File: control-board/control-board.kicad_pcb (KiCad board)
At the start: 2 copper layers, 218 x 137.7 mm, 639 parts, among them J1 LED ch 1-24, J10 ESP32 left (3V3 row), J11 ESP32 right (GND row), J2 LED ch 25-48, J3 LED ch 49-72, J4 LED ch 73-96, J5 logic/analog, J6 24V IN, J7 24V IN (5.5/2.5), J8 FAN 24V, Q1 AO3400A, SW1 MODE, SW2 UP, SW3 DOWN, U1 PT4115, U10 PT4115, U101 PCA9685PW (0x40), U102 PCA9685PW (0x41), U103 PCA9685PW (0x42), U104 PCA9685PW (0x43), U105 PCA9685PW (0x44), U106 PCA9685PW (0x45), U11 PT4115, U110 XL1509-5.0E1, U111 ADS1115IDGS (DNP), U12 PT4115, U13 PT4115, U14 PT4115, U15 PT4115, U16 PT4115, U17 PT4115, U18 PT4115, U19 PT4115, U2 PT4115, U20 PT4115, U21 PT4115, U22 PT4115, U23 PT4115, U24 PT4115, U25 PT4115, U26 PT4115, U27 PT4115, U28 PT4115, U29 PT4115, U3 PT4115, U30 PT4115, U31 PT4115, U32 PT4115, U33 PT4115, U34 PT4115, U35 PT4115, U36 PT4115, U37 PT4115, U38 PT4115, U39 PT4115, U4 PT4115, U40 PT4115, U41 PT4115, U42 PT4115, U43 PT4115, U44 PT4115, U45 PT4115, U46 PT4115, U47 PT4115, U48 PT4115, U49 PT4115, U5 PT4115, U50 PT4115, U51 PT4115, U52 PT4115, U53 PT4115, U54 PT4115, U55 PT4115, U56 PT4115, U57 PT4115, U58 PT4115, U59 PT4115, U6 PT4115, U60 PT4115, U61 PT4115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

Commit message: Control board: bottom-half cells mirrored toward J3/J4, pulldowns in disjoint per-half columns, silk declutter (288 passive refs hidden, rest shrunk to 0.9mm); placement DRC clean
Co-Authored-By: Claude Fable 5 <noreply@anthropic.com>
Claude-Session: https://claude.ai/code/session_017oD54uh7Tvu54u9NPQNcZB
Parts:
- moved R185 11.2 mm to (174.2, 119.7)
- moved R186 11.2 mm to (162.2, 119.7)
- moved R187 11.2 mm to (150.2, 119.7)
- moved R188 11.2 mm to (138.2, 119.7)
- moved R189 11.2 mm to (126.2, 119.7)
- moved R190 11.2 mm to (114.2, 119.7)
- moved R191 11.2 mm to (102.2, 119.7)
- moved R192 11.2 mm to (90.2, 119.7)
- moved R193 11.2 mm to (78.2, 119.7)
- moved R194 11.2 mm to (66.2, 119.7)
- moved R195 11.2 mm to (54.2, 119.7)
- moved R196 11.2 mm to (42.2, 119.7)
- moved R149 11.1 mm to (174.2, 82.9)
- moved R150 11.1 mm to (162.2, 82.9)
- moved R151 11.1 mm to (150.2, 82.9)
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
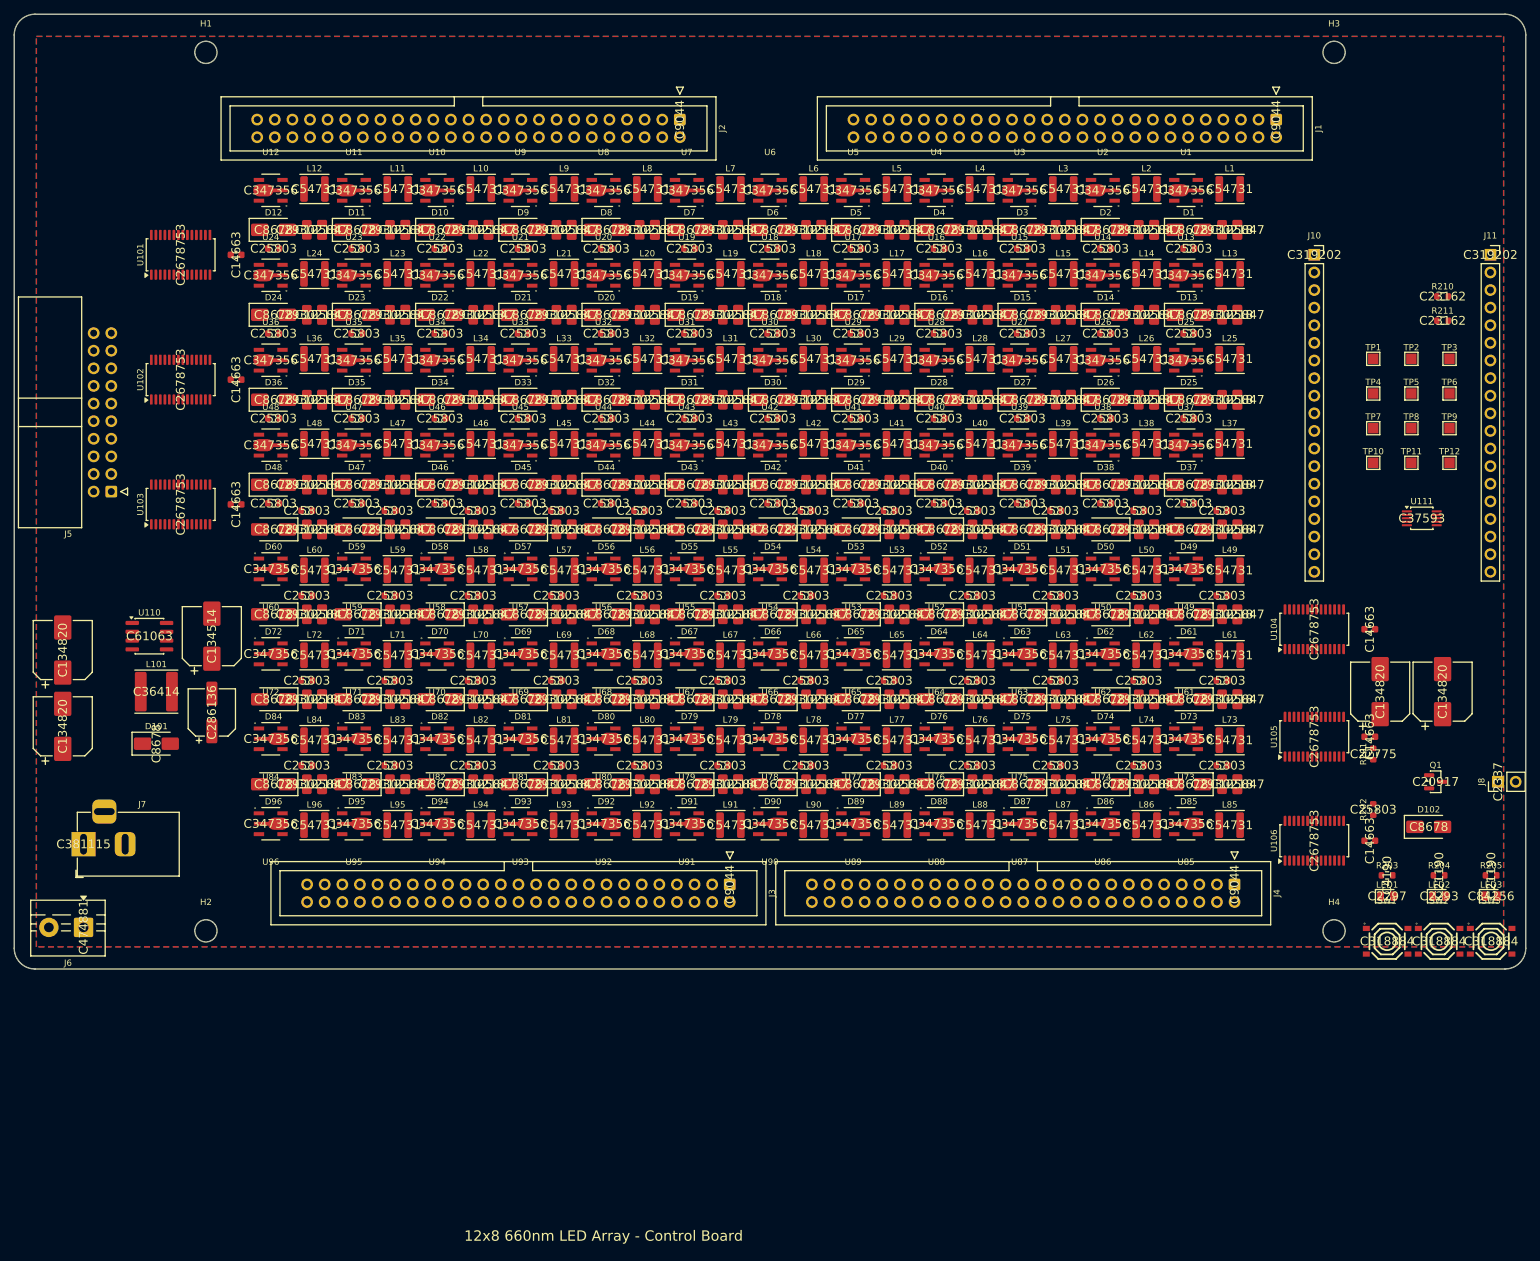
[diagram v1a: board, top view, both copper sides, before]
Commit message: Control board upgraded to 4-layer: In1 GND plane, In2 +24V plane
- Solid return plane under all 96 buck cells (EMI/return-path fix)
- 856 power stitching vias (every GND/+24V SMD pad -> its plane)
- Old 2-layer routing ripped; signals reroute on clean outer layers

Co-Authored-By: Claude Fable 5 <noreply@anthropic.com>
Claude-Session: https://claude.ai/code/session_017oD54uh7Tvu54u9NPQNcZB
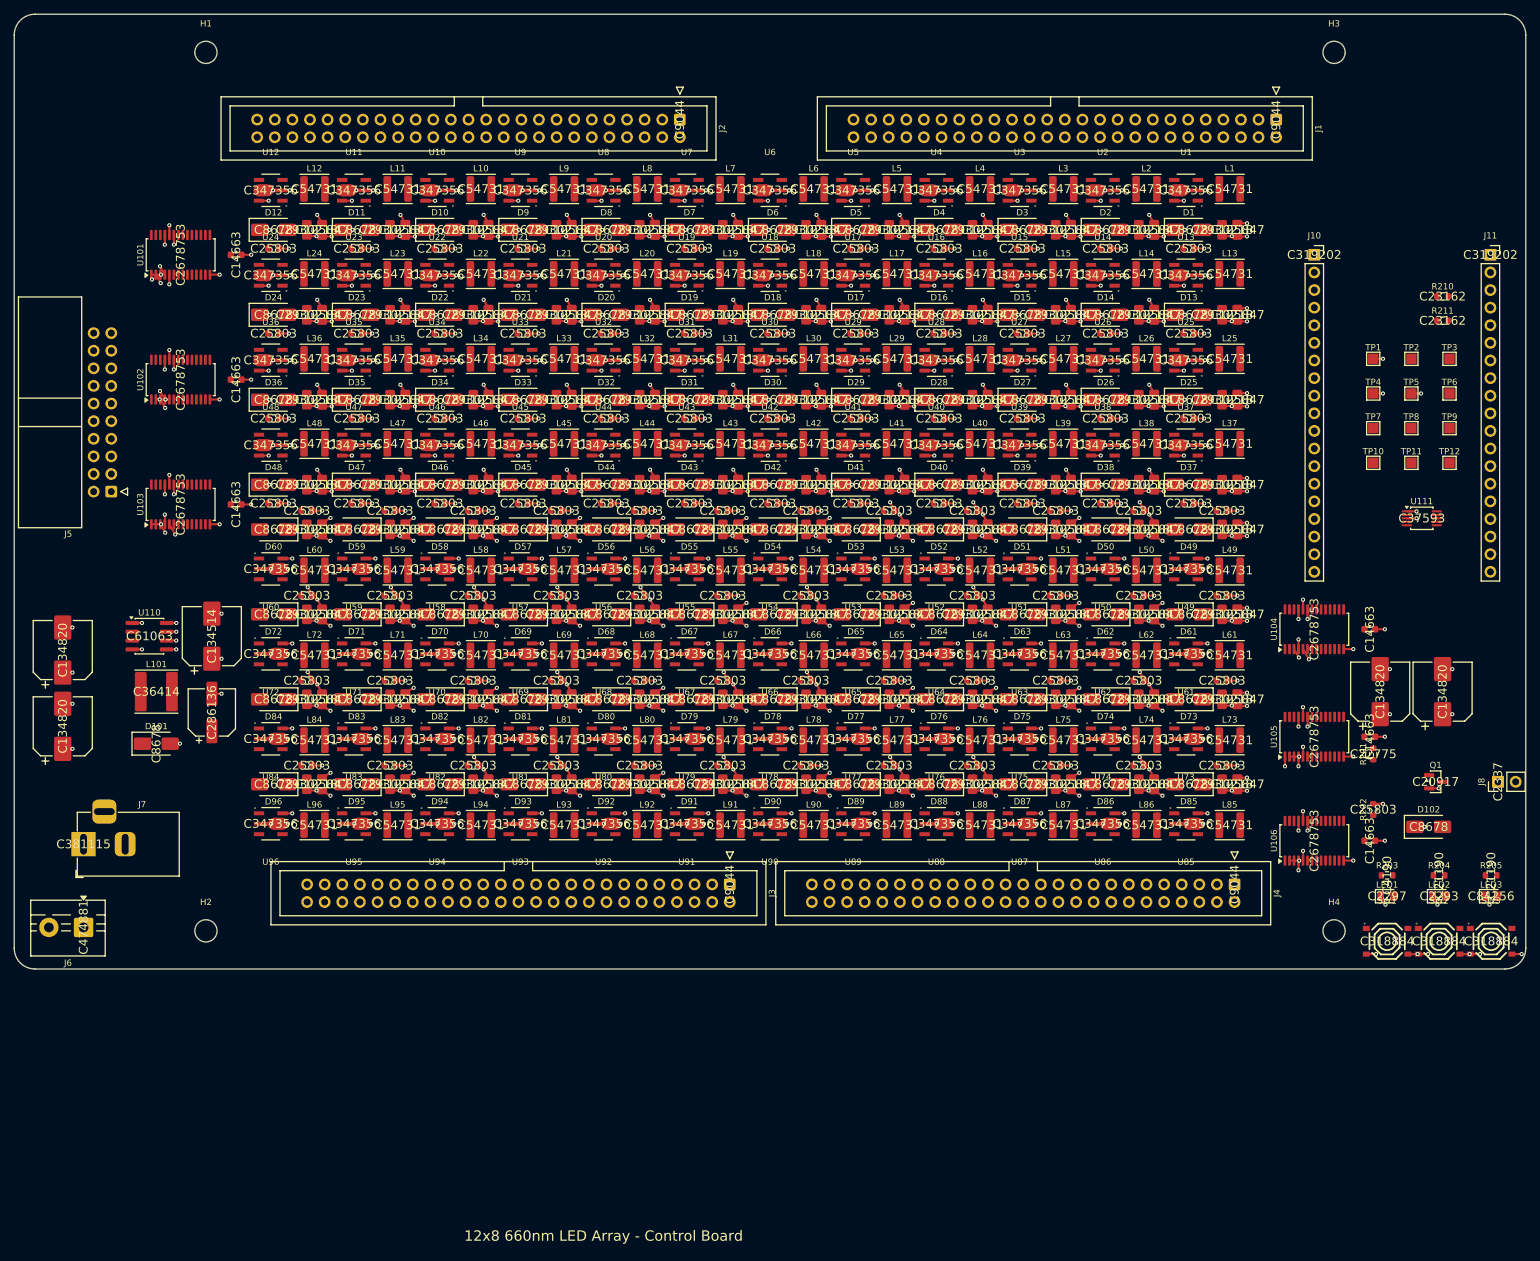
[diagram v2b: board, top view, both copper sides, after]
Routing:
- net GND: track 0.00 -> 650.2 mm, vias 0 -> 464
- net +24V: track 0.00 -> 548.8 mm, vias 0 -> 392
- added copper zone on In2.Cu, net +24V
- added copper zone on In1.Cu, net GND
- removed copper zone on F.Cu, net +24V
- removed copper zone on B.Cu, net GND
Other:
- copper layers 2 -> 4
